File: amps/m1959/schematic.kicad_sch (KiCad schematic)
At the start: 95 parts, among them T1 OT

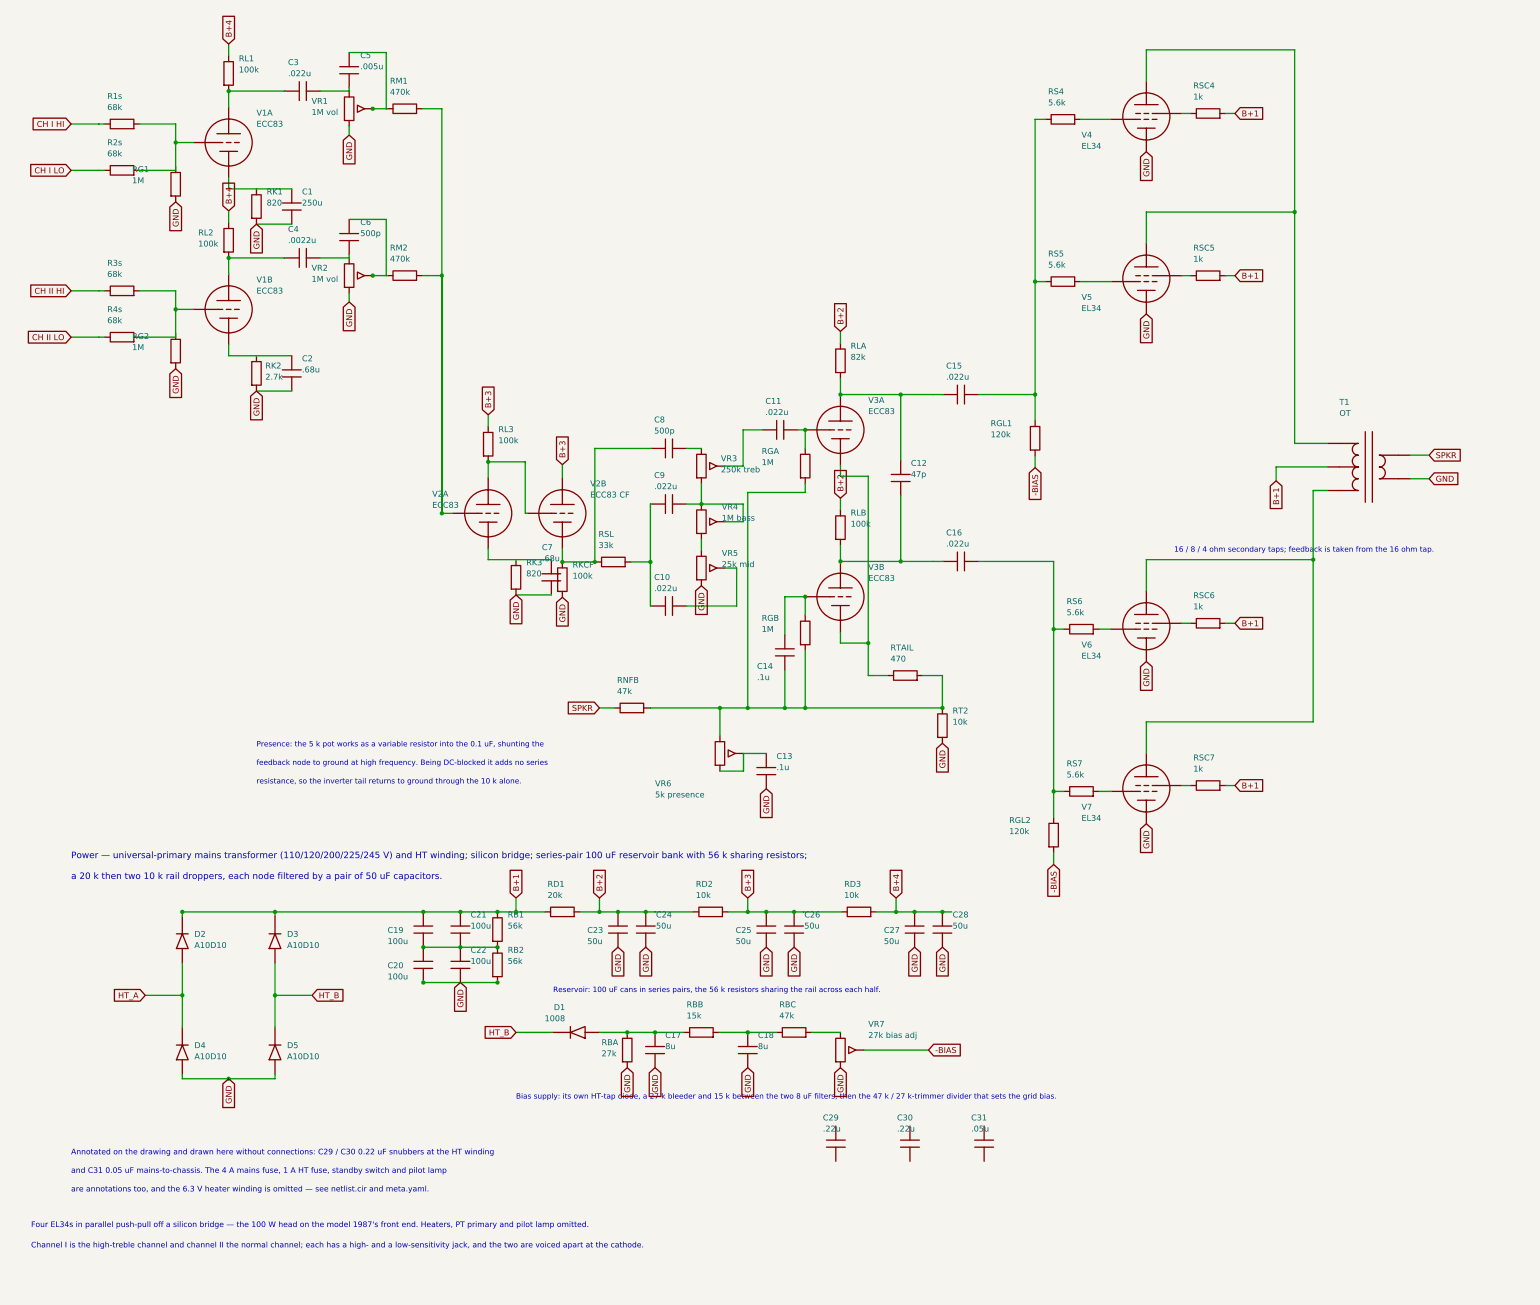
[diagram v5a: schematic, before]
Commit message: Fix: deterministic schematic ids and wires split at every join
- _u() is uuid5 over (amp id, emission order), so a regeneration of an
  unchanged script is byte-identical and a drift gate becomes possible
- write() splits wire segments at symbol pins, wire ends and junction dots,
  so the file connects exactly what the drawing shows under KiCad's
  endpoint-only semantics (270 pins were on a wire's interior; net
  partitions unchanged on all 38 sheets)
- all sheets regenerated; aa864-bassman title block was stale (draft) and
  now matches meta.yaml (verified)

Co-Authored-By: Claude Fable 5.1 <noreply@anthropic.com>
Claude-Session: https://claude.ai/code/session_01KBMfdh37HmCL2iWcBiL5J1
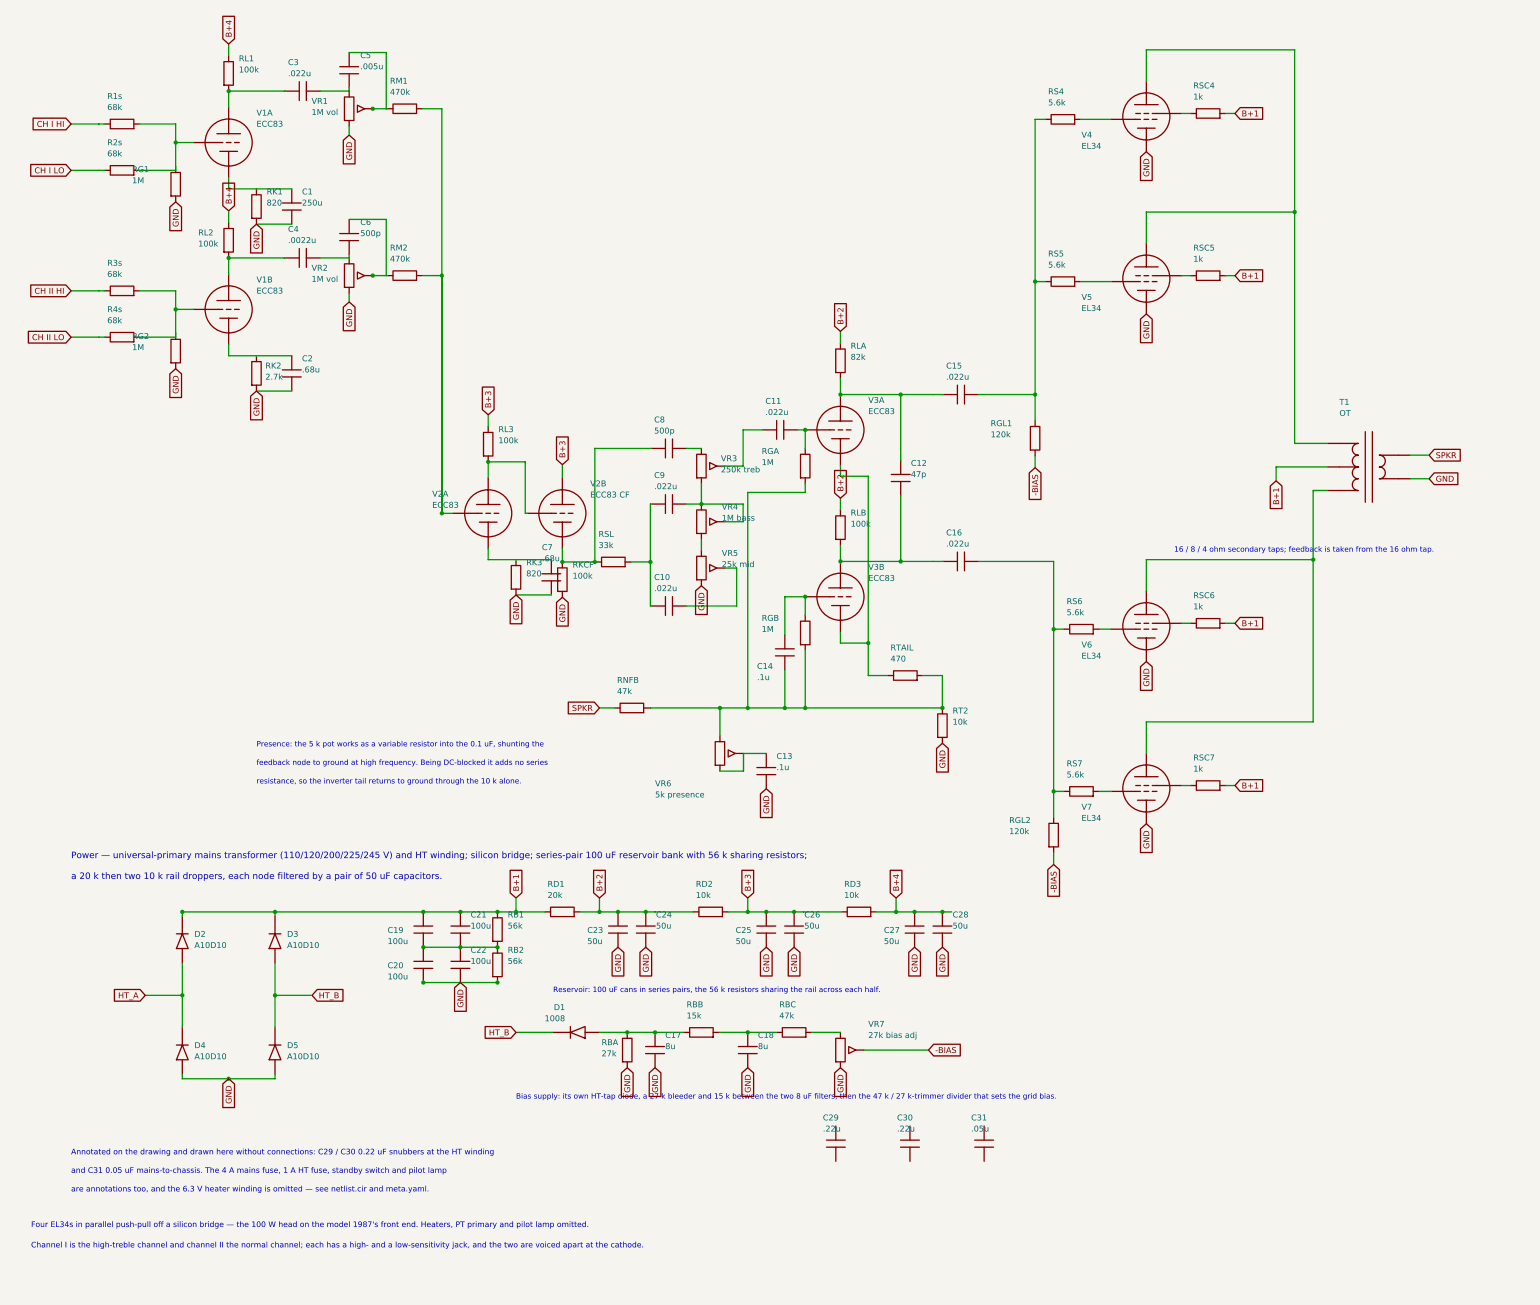
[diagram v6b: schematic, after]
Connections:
- net at RG1.1: now also R1s.2, R2s.2, V1A.2 (G)
- net at R3s.2, R4s.2, V1B.2 (G): now also RG2.1
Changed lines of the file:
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@@
   (wire (pts (xy 36.146 44.278) (xy 43.906 44.278))
     (stroke (width 0) (type default)))
-  (wire (pts (xy 43.906 44.278) (xy 43.906 38.278))
+  (wire (pts (xy 43.906 44.278) (xy 43.906 43.468))
+    (stroke (width 0) (type default)))
+  (wire (pts (xy 43.906 43.468) (xy 43.906 38.278))
     (stroke (width 0) (type default)))
   (junction (at 43.906 38.278) (diameter 0) (color 0 0 0 0))
@@
   (wire (pts (xy 97.146 30.988) (xy 101.336 30.988))
     (stroke (width 0) (type default)))
-  (wire (pts (xy 101.336 30.988) (xy 101.336 118.278))
+  (wire (pts (xy 101.336 30.988) (xy 101.336 66.988))
+    (stroke (width 0) (type default)))
+  (wire (pts (xy 101.336 66.988) (xy 101.336 118.278))
     (stroke (width 0) (type default)))
   (symbol (lib_id "cx:TRIODE") (at 55.336 74.278 0) (unit 1)
@@
   (wire (pts (xy 36.146 80.278) (xy 43.906 80.278))
     (stroke (width 0) (type default)))
-  (wire (pts (xy 43.906 80.278) (xy 43.906 74.278))
+  (wire (pts (xy 43.906 80.278) (xy 43.906 79.468))
+    (stroke (width 0) (type default)))
+  (wire (pts (xy 43.906 79.468) (xy 43.906 74.278))
     (stroke (width 0) (type default)))
   (junction (at 43.906 74.278) (diameter 0) (color 0 0 0 0))
@@
   (wire (pts (xy 166.336 100.278) (xy 170.526 100.278))
     (stroke (width 0) (type default)))
-  (wire (pts (xy 178.146 100.278) (xy 179.736 100.278))
+  (wire (pts (xy 178.146 100.278) (xy 179.716 100.278))
+    (stroke (width 0) (type default)))
+  (wire (pts (xy 179.716 100.278) (xy 179.736 100.278))
     (stroke (width 0) (type default)))
   (symbol (lib_id "cx:TRIODE") (at 187.336 100.278 0) (unit 1)
@@
   (wire (pts (xy 187.336 146.278) (xy 193.336 146.278))
     (stroke (width 0) (type default)))
-  (wire (pts (xy 193.336 110.278) (xy 193.336 153.278))
+  (wire (pts (xy 193.336 110.278) (xy 193.336 146.278))
+    (stroke (width 0) (type default)))
+  (wire (pts (xy 193.336 146.278) (xy 193.336 153.278))
     (stroke (width 0) (type default)))
   (junction (at 193.336 146.278) (diameter 0) (color 0 0 0 0))
@@
   (wire (pts (xy 179.736 136.278) (xy 179.716 136.278))
     (stroke (width 0) (type default)))
-  (wire (pts (xy 175.336 136.278) (xy 179.736 136.278))
+  (wire (pts (xy 175.336 136.278) (xy 179.716 136.278))
+    (stroke (width 0) (type default)))
+  (wire (pts (xy 179.716 136.278) (xy 179.736 136.278))
     (stroke (width 0) (type default)))
   (wire (pts (xy 175.336 136.278) (xy 175.336 144.468))
@@
   (wire (pts (xy 175.336 152.088) (xy 175.336 160.278))
     (stroke (width 0) (type default)))
-  (wire (pts (xy 146.336 160.278) (xy 167.336 160.278))
+  (wire (pts (xy 146.336 160.278) (xy 161.336 160.278))
+    (stroke (width 0) (type default)))
+  (wire (pts (xy 161.336 160.278) (xy 167.336 160.278))
     (stroke (width 0) (type default)))
   (wire (pts (xy 167.336 160.278) (xy 175.336 160.278))
@@
   (wire (pts (xy 217.146 92.658) (xy 229.336 92.658))
     (stroke (width 0) (type default)))
-  (wire (pts (xy 229.336 33.278) (xy 229.336 92.658))
+  (wire (pts (xy 229.336 33.278) (xy 229.336 68.278))
+    (stroke (width 0) (type default)))
+  (wire (pts (xy 229.336 68.278) (xy 229.336 92.658))
     (stroke (width 0) (type default)))
   (junction (at 229.336 68.278) (diameter 0) (color 0 0 0 0))
@@
   (wire (pts (xy 217.146 128.658) (xy 233.336 128.658))
     (stroke (width 0) (type default)))
-  (wire (pts (xy 233.336 128.658) (xy 233.336 178.278))
+  (wire (pts (xy 233.336 128.658) (xy 233.336 143.278))
+    (stroke (width 0) (type default)))
+  (wire (pts (xy 233.336 143.278) (xy 233.336 178.278))
     (stroke (width 0) (type default)))
   (junction (at 233.336 143.278) (diameter 0) (color 0 0 0 0))
@@
   (wire (pts (xy 253.336 18.278) (xy 285.336 18.278))
     (stroke (width 0) (type default)))
-  (wire (pts (xy 285.336 18.278) (xy 285.336 103.198))
+  (wire (pts (xy 285.336 18.278) (xy 285.336 53.278))
+    (stroke (width 0) (type default)))
+  (wire (pts (xy 285.336 53.278) (xy 285.336 103.198))
     (stroke (width 0) (type default)))
   (wire (pts (xy 253.336 60.023) (xy 253.336 53.278))
@@
   (wire (pts (xy 253.336 163.278) (xy 289.336 163.278))
     (stroke (width 0) (type default)))
-  (wire (pts (xy 289.336 163.278) (xy 289.336 113.358))
+  (wire (pts (xy 289.336 163.278) (xy 289.336 128.278))
+    (stroke (width 0) (type default)))
+  (wire (pts (xy 289.336 128.278) (xy 289.336 113.358))
     (stroke (width 0) (type default)))
   (junction (at 289.336 128.278) (diameter 0) (color 0 0 0 0))
@@
   (wire (pts (xy 45.336 204.278) (xy 65.336 204.278))
     (stroke (width 0) (type default)))
-  (wire (pts (xy 45.336 240.278) (xy 65.336 240.278))
+  (wire (pts (xy 45.336 240.278) (xy 55.336 240.278))
+    (stroke (width 0) (type default)))
+  (wire (pts (xy 55.336 240.278) (xy 65.336 240.278))
     (stroke (width 0) (type default)))
   (global_label "GND" (shape input) (at 55.336 240.278 270)
     (effects (font (size 1.27 1.27)) (justify right)))
   (junction (at 55.336 240.278) (diameter 0) (color 0 0 0 0))
-  (wire (pts (xy 65.336 204.278) (xy 117.336 204.278))
+  (wire (pts (xy 65.336 204.278) (xy 97.336 204.278))
+    (stroke (width 0) (type default)))
+  (wire (pts (xy 97.336 204.278) (xy 105.336 204.278))
+    (stroke (width 0) (type default)))
+  (wire (pts (xy 105.336 204.278) (xy 113.336 204.278))
+    (stroke (width 0) (type default)))
+  (wire (pts (xy 113.336 204.278) (xy 117.336 204.278))
     (stroke (width 0) (type default)))
   (symbol (lib_id "cx:C") (at 97.336 208.088 0) (unit 1)
@@
   (junction (at 113.336 204.278) (diameter 0) (color 0 0 0 0))
   (junction (at 113.336 211.898) (diameter 0) (color 0 0 0 0))
-  (wire (pts (xy 97.336 211.898) (xy 113.336 211.898))
-    (stroke (width 0) (type default)))
-  (wire (pts (xy 97.336 219.518) (xy 113.336 219.518))
+  (wire (pts (xy 97.336 211.898) (xy 105.336 211.898))
+    (stroke (width 0) (type default)))
+  (wire (pts (xy 105.336 211.898) (xy 113.336 211.898))
+    (stroke (width 0) (type default)))
+  (wire (pts (xy 97.336 219.518) (xy 105.336 219.518))
+    (stroke (width 0) (type default)))
+  (wire (pts (xy 105.336 219.518) (xy 113.336 219.518))
     (stroke (width 0) (type default)))
   (global_label "GND" (shape input) (at 105.336 219.518 270)
@@
     (property "Reference" "RD1" (at 124.136 198.278 270) (effects (font (size 1.27 1.27)) (justify left)))
     (property "Value" "20k" (at 124.136 200.678 270) (effects (font (size 1.27 1.27)) (justify left))))
-  (wire (pts (xy 131.146 204.278) (xy 147.336 204.278))
+  (wire (pts (xy 131.146 204.278) (xy 135.336 204.278))
+    (stroke (width 0) (type default)))
+  (wire (pts (xy 135.336 204.278) (xy 139.336 204.278))
+    (stroke (width 0) (type default)))
+  (wire (pts (xy 139.336 204.278) (xy 145.336 204.278))
+    (stroke (width 0) (type default)))
+  (wire (pts (xy 145.336 204.278) (xy 147.336 204.278))
     (stroke (width 0) (type default)))
   (junction (at 135.336 204.278) (diameter 0) (color 0 0 0 0))
@@
     (property "Reference" "RD2" (at 156.136 198.278 270) (effects (font (size 1.27 1.27)) (justify left)))
     (property "Value" "10k" (at 156.136 200.678 270) (effects (font (size 1.27 1.27)) (justify left))))
-  (wire (pts (xy 163.146 204.278) (xy 179.336 204.278))
+  (wire (pts (xy 163.146 204.278) (xy 167.336 204.278))
+    (stroke (width 0) (type default)))
+  (wire (pts (xy 167.336 204.278) (xy 171.336 204.278))
+    (stroke (width 0) (type default)))
+  (wire (pts (xy 171.336 204.278) (xy 177.336 204.278))
+    (stroke (width 0) (type default)))
+  (wire (pts (xy 177.336 204.278) (xy 179.336 204.278))
     (stroke (width 0) (type default)))
   (junction (at 167.336 204.278) (diameter 0) (color 0 0 0 0))
@@
     (property "Reference" "RD3" (at 188.136 198.278 270) (effects (font (size 1.27 1.27)) (justify left)))
     (property "Value" "10k" (at 188.136 200.678 270) (effects (font (size 1.27 1.27)) (justify left))))
-  (wire (pts (xy 195.146 204.278) (xy 211.336 204.278))
+  (wire (pts (xy 195.146 204.278) (xy 199.336 204.278))
+    (stroke (width 0) (type default)))
+  (wire (pts (xy 199.336 204.278) (xy 203.336 204.278))
+    (stroke (width 0) (type default)))
+  (wire (pts (xy 203.336 204.278) (xy 209.336 204.278))
+    (stroke (width 0) (type default)))
+  (wire (pts (xy 209.336 204.278) (xy 211.336 204.278))
     (stroke (width 0) (type default)))
   (junction (at 199.336 204.278) (diameter 0) (color 0 0 0 0))
@@
     (property "Reference" "D1" (at 127.936 224.878 0) (effects (font (size 1.27 1.27)) (justify left)))
     (property "Value" "1008" (at 127.936 227.278 0) (effects (font (size 1.27 1.27)) (justify left))))
-  (wire (pts (xy 135.416 230.278) (xy 147.336 230.278))
+  (wire (pts (xy 135.416 230.278) (xy 141.336 230.278))
+    (stroke (width 0) (type default)))
+  (wire (pts (xy 141.336 230.278) (xy 147.336 230.278))
     (stroke (width 0) (type default)))
   (junction (at 141.336 230.278) (diameter 0) (color 0 0 0 0))

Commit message: Fix: schematic wiring on m1987, aa864-bassman, ac30, m1959, ga40, aa1164, aa964
- 58 open pins closed: leads that stopped short of their flags, pins
  missed by 0.01-0.11 mm, snubbers and bright caps with no leads
- two shorts the isolated-pin check cannot see: aa864-bassman V6 anode
  lead ran through its grounded cathode (plate rail to chassis) and its V5
  coupler drop shorted RGL1; m1987 RB1/RB2 stood on the wire they bridge
- 14 dated waivers: m1959 C29-C31 (factory sheet prints them unconnected),
  ga40 V2/V3/VR3.3 (net_map excluded tubes, free rheostat lug)
- all seven sheets pass connectivity and verify_schematic_nets

Co-Authored-By: Claude Fable 5.1 <noreply@anthropic.com>
Claude-Session: https://claude.ai/code/session_01KBMfdh37HmCL2iWcBiL5J1
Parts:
- removed C31: .05u, symbol cx:C
- added C29: .22u, symbol cx:C
- C31: renamed from C30; value .22u -> .05u
- renumbered C29 to C30
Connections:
- net at C5.1, RM1.1: now also VR1.2 (W)
- net at C6.1, RM2.1: now also VR2.2 (W)
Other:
- moved on the sheet: C30, C31
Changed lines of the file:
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@@
   (wire (pts (xy 89.336 18.868) (xy 89.336 30.988))
     (stroke (width 0) (type default)))
-  (junction (at 86.426 30.988) (diameter 0) (color 0 0 0 0))
-  (wire (pts (xy 86.426 30.988) (xy 89.336 30.988))
+  (junction (at 86.416 30.988) (diameter 0) (color 0 0 0 0))
+  (wire (pts (xy 86.416 30.988) (xy 89.336 30.988))
     (stroke (width 0) (type default)))
   (symbol (lib_id "cx:R") (at 93.336 30.988 90) (unit 1)
@@
   (wire (pts (xy 89.336 54.868) (xy 89.336 66.988))
     (stroke (width 0) (type default)))
-  (junction (at 86.426 66.988) (diameter 0) (color 0 0 0 0))
-  (wire (pts (xy 86.426 66.988) (xy 89.336 66.988))
+  (junction (at 86.416 66.988) (diameter 0) (color 0 0 0 0))
+  (wire (pts (xy 86.416 66.988) (xy 89.336 66.988))
     (stroke (width 0) (type default)))
   (symbol (lib_id "cx:R") (at 93.336 66.988 90) (unit 1)
@@
   (wire (pts (xy 203.336 204.278) (xy 209.336 204.278))
     (stroke (width 0) (type default)))
-  (wire (pts (xy 209.336 204.278) (xy 211.336 204.278))
-    (stroke (width 0) (type default)))
   (junction (at 199.336 204.278) (diameter 0) (color 0 0 0 0))

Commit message: Add: real tube pin numbers and readable valve glyphs on every schematic
Phase B of the drawing program. A factory service sheet numbers every tube
pin, because the number is what a technician puts a probe on. This corpus
printed none, and the numbers hidden in its symbols were positional
placeholders (P=1, G=2, K=3) that would have published a 6V6GT's plate as
pin 1 when it is pin 3.

1055 electrodes now carry the real number, 1027 lettered (27 are shared
filaments deduped, 1 dropped for want of clear space on the 6G2). Resolved per
instance from reference/tubes/<slug>.yaml through the same alias resolution the
layout renderer uses, so a 12AX7 section and a 6SL7 section each get their own
basing. A valve whose basing the corpus does not carry prints nothing rather
than a wrong number.

Section letters and basing units are now separate things, which cost a detour
worth recording. The RCA 12AX7-A sheet reads "Pin 1 - Plate of Unit No.2 ...
Pin 6 - Plate of Unit No.1", so unit numbering is not pin order; the 5Y3 and
GZ34 number their units in opposite pin order, so nothing positional can
express it. But the section LETTER is a designator, not a basing fact: this
corpus, like every technician, calls the first stage in signal order V1A, and
five amps' prose already did. On four amps the factory sheets put that first
stage on the other half -- the AA764's own schematic prints +200 V on pin 1 --
so those drawings now state their unit explicitly, each citing its source, and
no letter, netlist, parts list or layout comment changed. 183 layout comments
agree with the printed numbers, 0 disagree. A guard fires if two halves of one
bottle resolve to the same unit, which is exactly how this was found.

Glyphs: the cathode gains a bracket and filament hairpin so it can no longer be
confused with the plate bar, the pentode's screen sits on its own row, and a
rectifier draws as one envelope over its sections instead of two apparent
bottles. Line weights are scaled per sheet to a co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
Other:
- note added: "1"
- note added: "2"
- note added: "3"
- note added: "4"
- note added: "5"
- note added: "6"
- note added: "7"
- note added: "8"
